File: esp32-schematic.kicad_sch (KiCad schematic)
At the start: 21 parts, among them J1 GN-2630G, J2 Jumper, J3 Micro_SD_Card, U1 ESP32-S3-DEVKITC-1U-N8R2, U2 TJA1051T, U4 MPU-9250

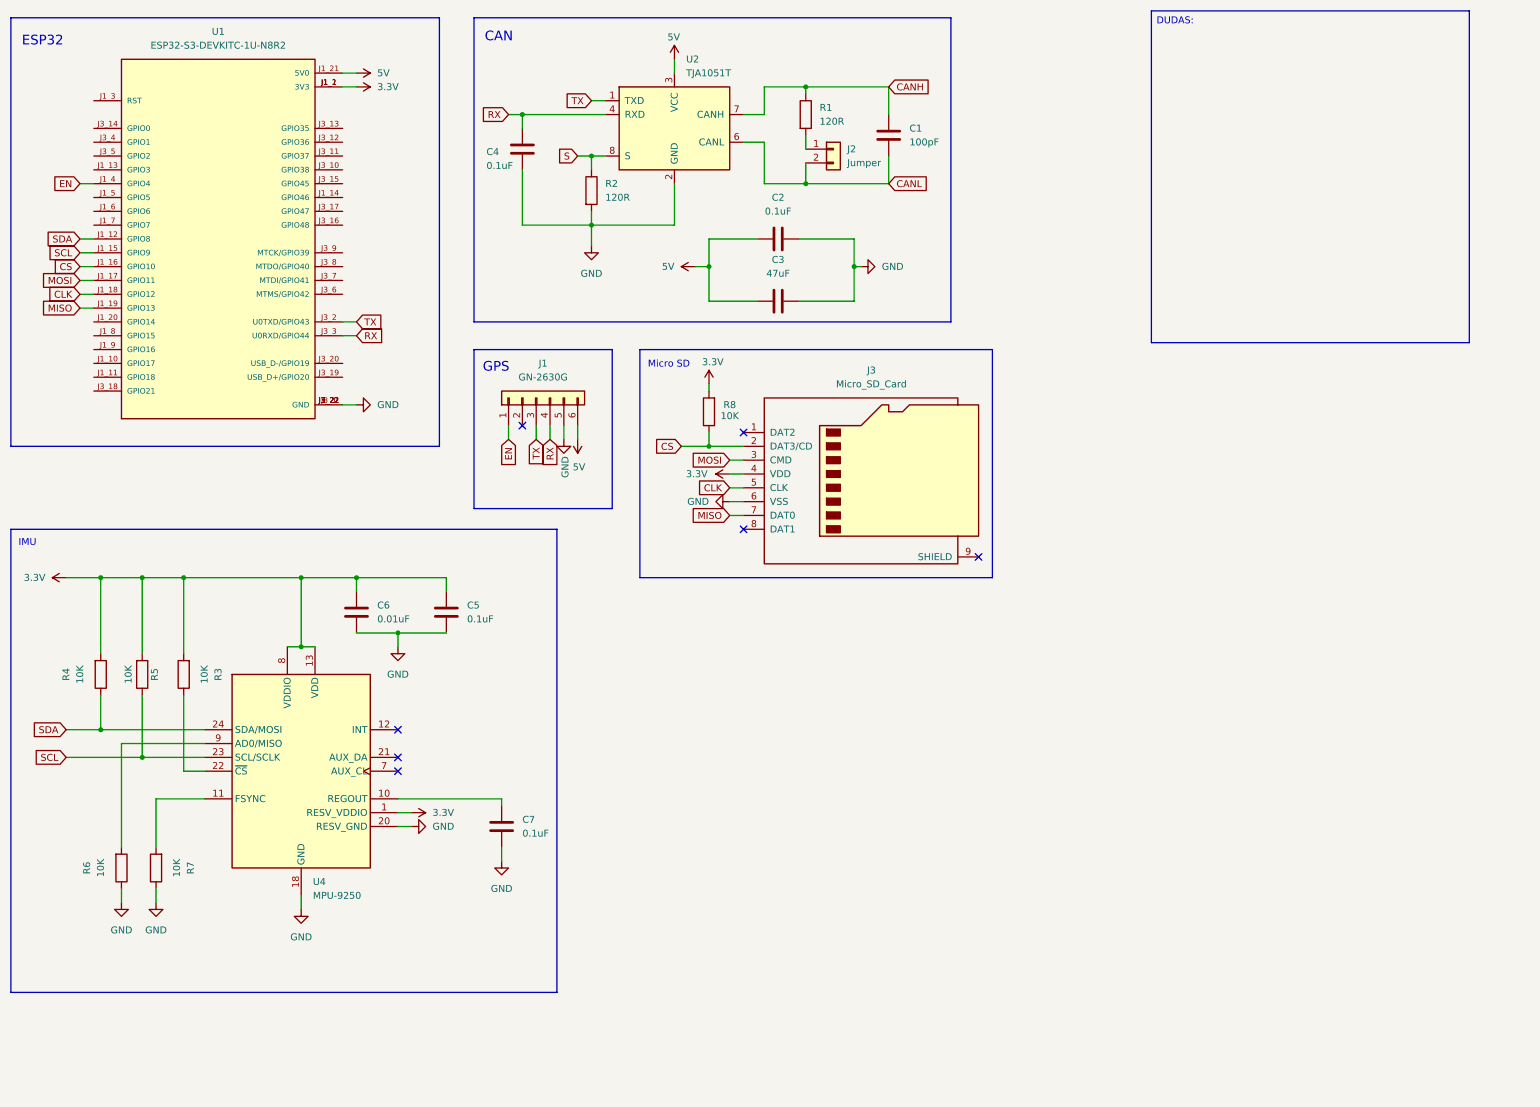
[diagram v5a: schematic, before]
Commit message: SD slot added, ENV added, issues fixed
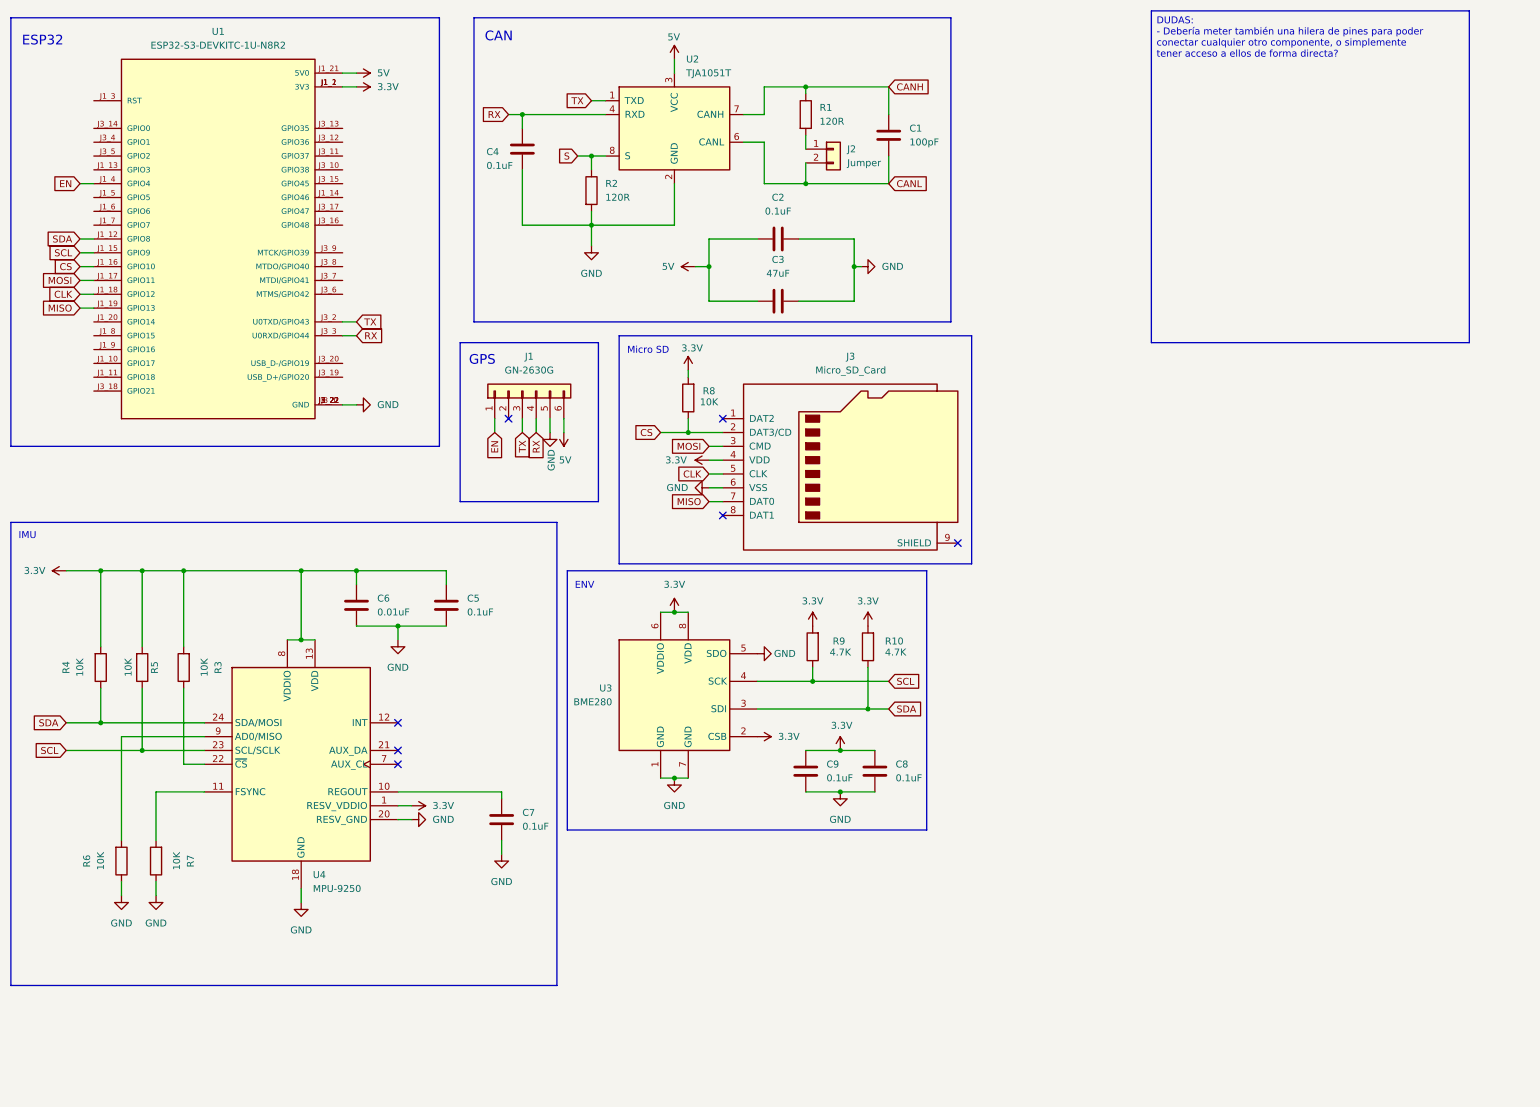
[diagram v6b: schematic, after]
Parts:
- added C8, C9: 0.1uF, Capacitor_SMD:C_0805_2012Metric, symbol Device:C
- added R10, R9: 4.7K, Resistor_SMD:R_1206_3216Metric, symbol Device:R
- added U3: BME280, Package_LGA:Bosch_LGA-8_2.5x2.5mm_P0.65mm_ClockwisePinNumbering, symbol Sensor:BME280
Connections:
- net 3.3V: now also C8.1, C9.1, R10.2, R9.2, U3.2 (CSB), U3.6 (VDDIO), U3.8 (VDD)
- net GND: now also C8.2, C9.2, U3.1 (GND), U3.5 (SDO), U3.7 (GND)
- net SCL: now also R9.1, U3.4 (SCK)
- net SDA: now also R10.1, U3.3 (SDI)
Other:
- note added: "ENV"
- moved on the sheet: C5, C6, C7, J1, J3, R3, R4, R5, R6, R7, R8, U4

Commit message: DC-DC added, and bornes for the esp32 in progress
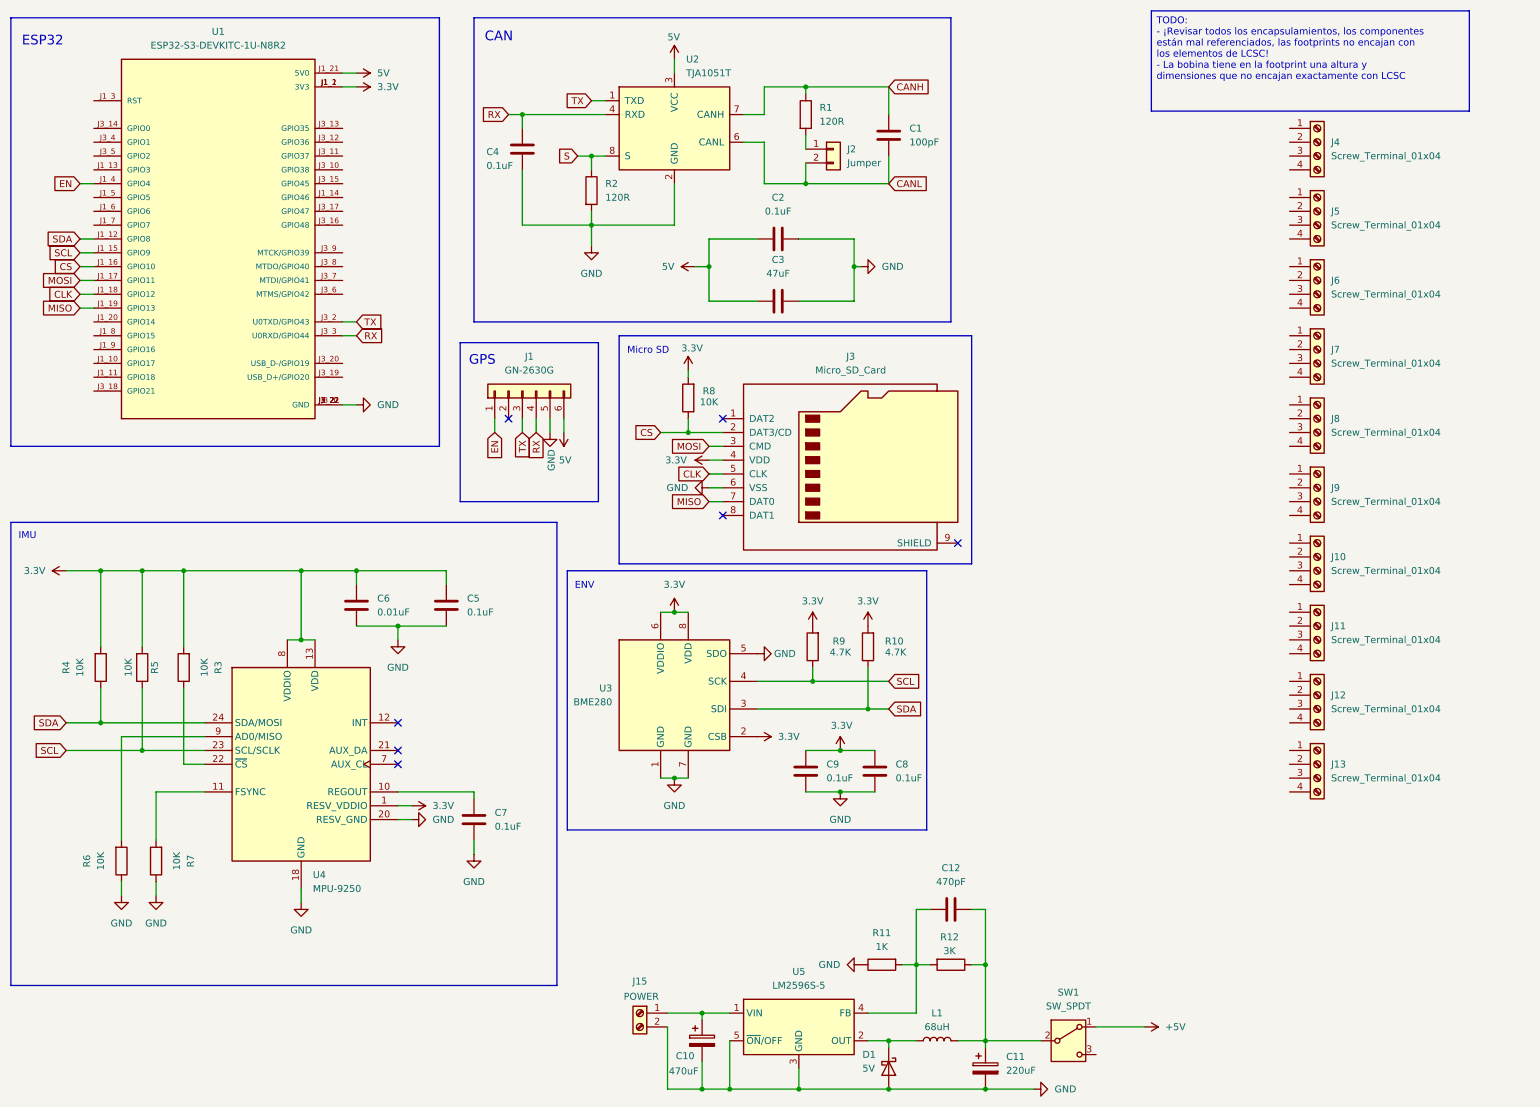
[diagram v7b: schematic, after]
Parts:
- added C10: 470uF, Capacitor_THT:CP_Radial_D10.0mm_P5.00mm, symbol Device:C_Polarized
- added C11: 220uF, Capacitor_SMD:CP_Elec_10x10, symbol Device:C_Polarized
- added C12: 470pF, Capacitor_SMD:C_0201_0603Metric, symbol Device:C
- added D1: 5V, Diode_SMD:D_SMA, symbol Device:D_Schottky
- added J10, J11, J12, J13, J4, J5, J6, J7, J8, J9: Screw_Terminal_01x04, TerminalBlock_Phoenix:TerminalBlock_Phoenix_MKDS-1,5-4-5.08_1x04_P5.08mm_Horizontal, symbol Connector:Screw_Terminal_01x04
- added J15: POWER, TerminalBlock_Phoenix:TerminalBlock_Phoenix_PT-1,5-2-3.5-H_1x02_P3.50mm_Horizontal, symbol Connector:Screw_Terminal_01x02
- added L1: 68uH, Inductor_SMD:L_12x12mm_H6mm, symbol Device:L
- added R11: 1K, Resistor_SMD:R_0201_0603Metric, symbol Device:R
- added R12: 3K, Resistor_THT:R_Axial_DIN0411_L9.9mm_D3.6mm_P15.24mm_Horizontal, symbol Device:R
- added SW1: SW_SPDT, Button_Switch_SMD:SW_DPDT_CK_JS202011JCQN, symbol Switch:SW_SPDT
- added U5: LM2596S-5, Package_TO_SOT_SMD:TO-263-5_TabPin3, symbol Regulator_Switching:LM2596S-5
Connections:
- net GND: now also C10.2, C11.2, D1.2 (A), J15.2 (Pin_2), R11.1, U5.3 (GND), U5.5 (~{ON}/OFF)
- new net: C10.1, J15.1 (Pin_1), U5.1 (VIN)
- new net: D1.1 (K), L1.1, U5.2 (OUT)
- new net: C12.1, R11.2, R12.2, U5.4 (FB)
- new net: C11.1, C12.2, L1.2, R12.1, SW1.2 (B)
- new net +5V: SW1.1 (A)
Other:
- moved on the sheet: C7
